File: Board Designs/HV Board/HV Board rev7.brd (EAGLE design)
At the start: 118.6 x 71.4 mm, 58 parts, among them IC1 OKI-78SR, IC2 NE5532SOIC

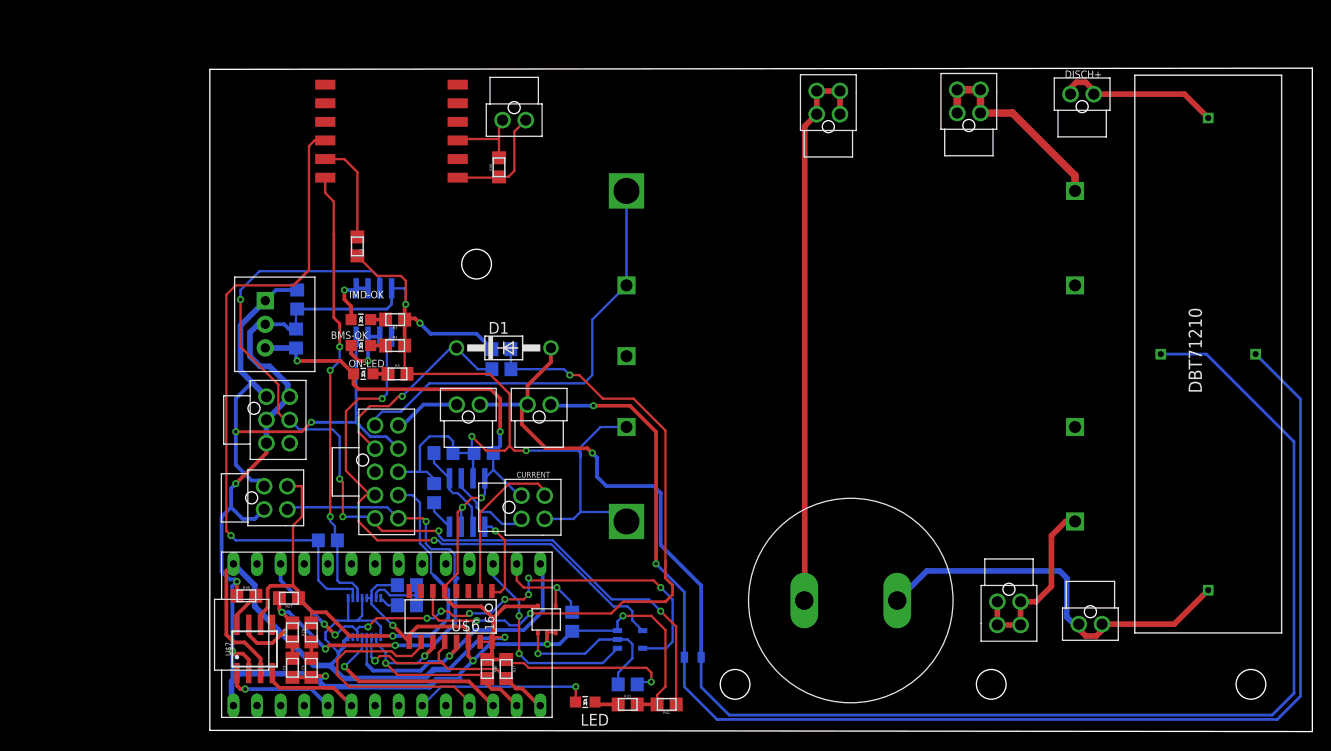
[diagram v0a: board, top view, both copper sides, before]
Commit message: Updated cynergy relay in lib, fixed DRC issues
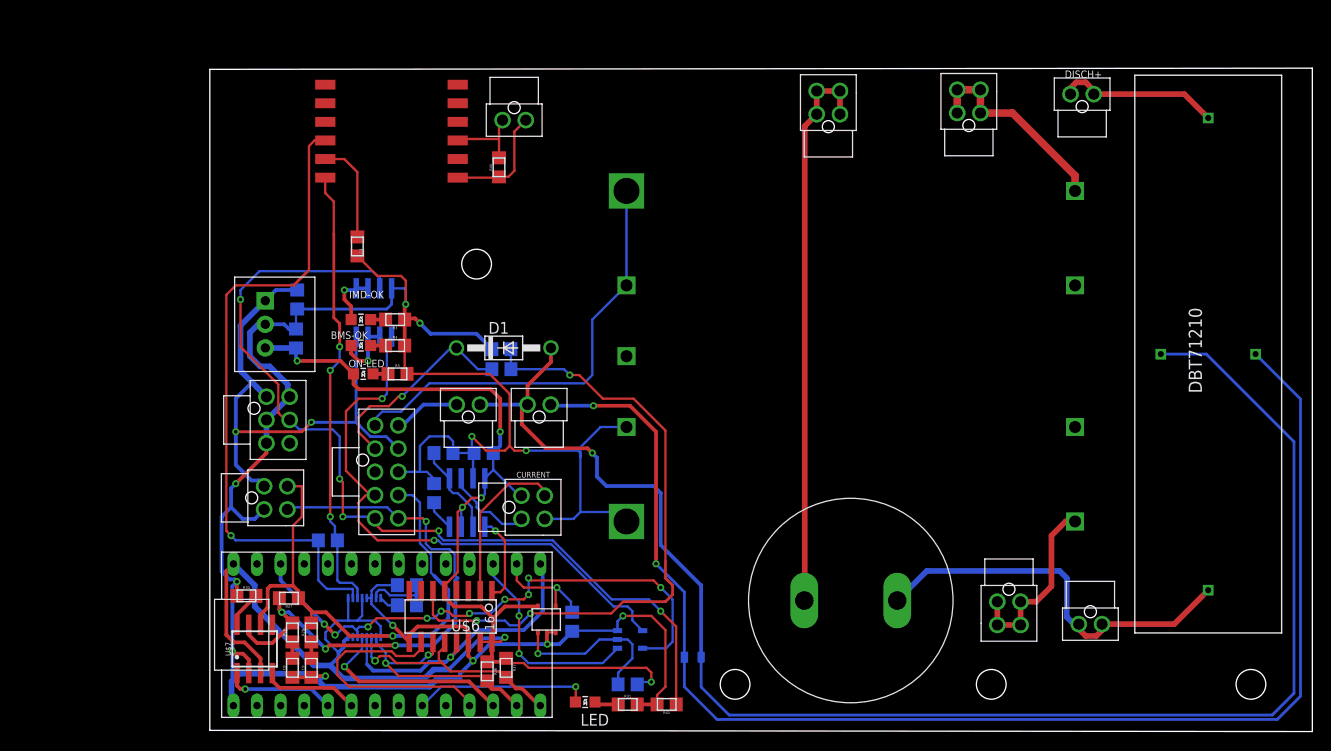
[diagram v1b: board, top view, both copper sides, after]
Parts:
- moved R36 0.25 mm to (50.4, 1.14)
- moved R37 0.13 mm to (52.5, 1.52)
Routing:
- net N$24: track 70.7 -> 69.7 mm
- net MOSI: track 26.0 -> 26.8 mm
- net N$34: track 48.8 -> 48.3 mm

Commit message: Moved 6820 next to transformer
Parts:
- IMD: value IMD -> CONNECTOR-6NANO-FIT_VERTICAL-6
- moved HV-FUSED_1A-IMD- 53.9 mm to (94.9, 61.2), turned to 0 degrees
- moved R33 38.5 mm to (31.4, 45.3), turned to 0 degrees
- moved R34 34.4 mm to (31.4, 43.2), turned to 180 degrees
- moved U$8 32.7 mm to (30.4, 37.0)
- moved R35 28.5 mm to (27.4, 43.2)
- moved C2 8.13 mm to (38.1, 41.4)
- moved C3 8.13 mm to (38.0, 37.2)
- moved IC1 8.13 mm to (34.7, 38.7)
- moved C1 6.54 mm to (96.0, 9.76)
- moved BMS-OK 5.35 mm to (42.2, 36.6)
- moved IC2 5.35 mm to (43.6, 40.1)
- moved IMD-OK 5.35 mm to (42.2, 39.4)
- moved R3 5.35 mm to (45.8, 39.4)
- moved R4 5.35 mm to (45.8, 36.6)
- moved ON-LED 5.35 mm to (42.4, 33.5)
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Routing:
- net N$33: track 70.4 -> 21.1 mm
- net CS_LTC6820: track 21.7 -> 64.0 mm
- net HV-FUSED_1A: track 20.6 -> 61.9 mm
- net SCK: track 31.9 -> 69.1 mm
- net MISO: track 25.7 -> 61.2 mm
- net MOSI: track 26.8 -> 61.5 mm
- net N$34: track 48.3 -> 15.8 mm, vias 3 -> 1
- net +3V3: track 60.5 -> 87.7 mm, vias 10 -> 8
- net GND: track 271.2 -> 249.5 mm
- net HV+UNFUSED: track 42.9 -> 29.4 mm
- net +5V: track 171.9 -> 159.3 mm
- net OKHS: track 98.3 -> 86.2 mm, vias 5 -> 4
- net +12V: track 59.0 -> 54.7 mm, vias 2 -> 1
- net N$31: track 2.12 -> 5.79 mm
- net BMS_OK: track 62.3 -> 59.1 mm
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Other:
- outline, holes or cut-outs redrawn
- board text added: "IMD"

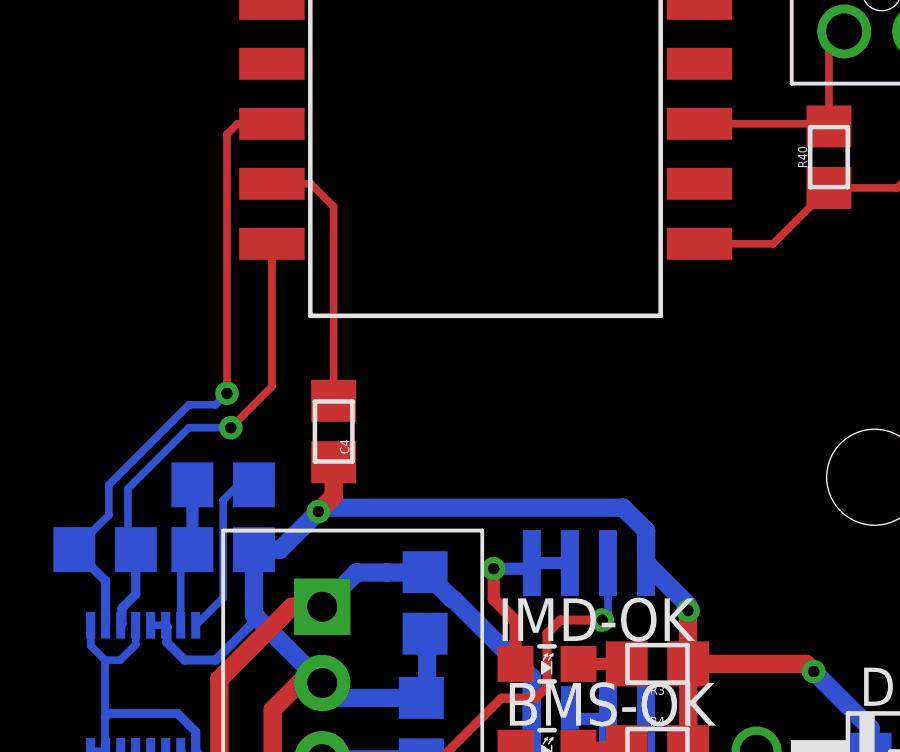
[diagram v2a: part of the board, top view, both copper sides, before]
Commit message: Moved resistor to clear space for the box
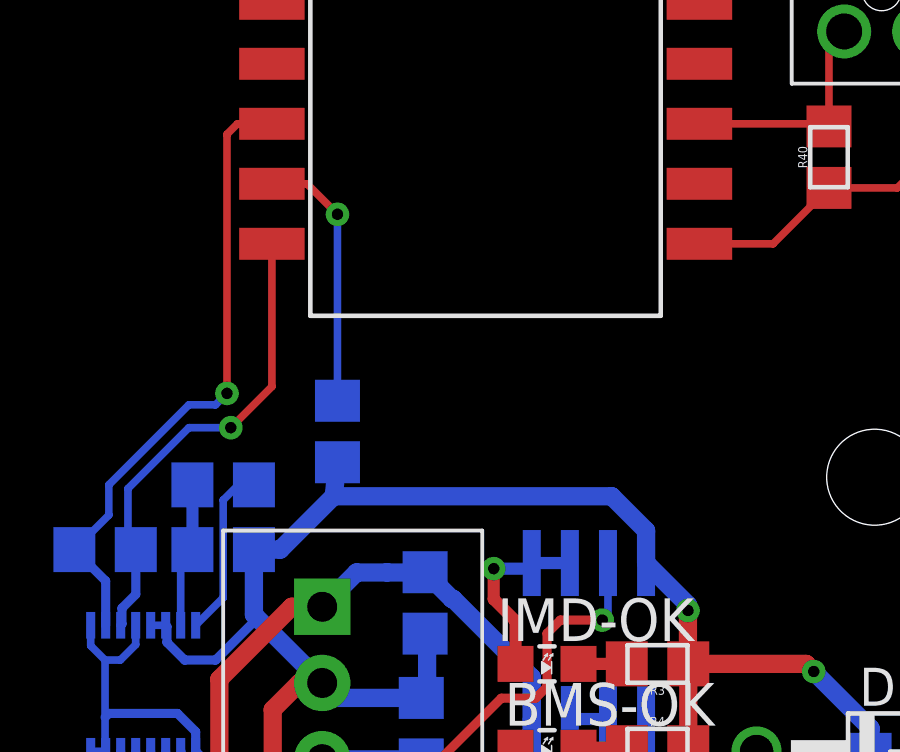
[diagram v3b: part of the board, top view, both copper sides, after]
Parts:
- moved C4 0.13 mm to (35.2, 47.1), flipped to the bottom
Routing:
- net GND: track 249.5 -> 249.1 mm, vias 12 -> 11
- net N$35: track 8.84 -> 8.82 mm, vias 0 -> 1
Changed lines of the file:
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@@
 <attribute name="VALUE" x="27.432" y="43.8912" size="0.3048" layer="28" rot="MR180" align="top-center"/>
 </element>
-<element name="C4" library="HyTechDevices" package="0805" value="27pF" x="35.052" y="47.117" smashed="yes" rot="R270">
-<attribute name="NAME" x="35.2679" y="46.609" size="0.3048" layer="25" rot="R270" align="bottom-center"/>
-<attribute name="VALUE" x="34.3408" y="47.117" size="0.3048" layer="27" rot="R270" align="top-center"/>
+<element name="C4" library="HyTechDevices" package="0805" value="27pF" x="35.179" y="47.117" smashed="yes" rot="MR270">
+<attribute name="NAME" x="34.9631" y="46.609" size="0.3048" layer="26" rot="MR270" align="bottom-center"/>
+<attribute name="VALUE" x="35.8902" y="47.117" size="0.3048" layer="28" rot="MR270" align="top-center"/>
 </element>
 <element name="R36" library="HyTechDevices" package="0805" value="2k" x="50.419" y="1.143" smashed="yes" rot="R270">
@@
 <wire x1="31.115" y1="39.497" x2="32.394" y2="40.776" width="0.3048" layer="16"/>
 <wire x1="32.394" y1="40.776" x2="32.394" y2="41.012" width="0.3048" layer="16"/>
-<wire x1="32.394" y1="43.18" x2="33.274" y2="43.18" width="0.6096" layer="16"/>
-<wire x1="33.274" y1="43.18" x2="34.544" y2="44.45" width="0.6096" layer="16"/>
-<via x="34.544" y="44.45" extent="1-16" drill="0.381"/>
-<wire x1="34.544" y1="44.45" x2="35.052" y2="44.958" width="0.6096" layer="1"/>
-<wire x1="35.052" y1="44.958" x2="35.052" y2="46.092" width="0.6096" layer="1"/>
-<wire x1="45.466" y1="42.732" x2="45.466" y2="43.815" width="0.6096" layer="16"/>
-<wire x1="45.466" y1="43.815" x2="44.704" y2="44.577" width="0.6096" layer="16"/>
-<wire x1="44.704" y1="44.577" x2="34.671" y2="44.577" width="0.6096" layer="16"/>
-<wire x1="34.671" y1="44.577" x2="34.544" y2="44.45" width="0.6096" layer="16"/>
+<wire x1="33.274" y1="43.18" x2="32.394" y2="43.18" width="0.6096" layer="16"/>
+<wire x1="35.179" y1="46.092" x2="35.052" y2="44.958" width="0.6096" layer="16"/>
+<wire x1="45.466" y1="43.815" x2="45.466" y2="42.732" width="0.6096" layer="16"/>
 <wire x1="45.466" y1="42.732" x2="46.863" y2="41.335" width="0.6096" layer="16"/>
 <wire x1="46.863" y1="41.335" x2="46.863" y2="41.148" width="0.6096" layer="16"/>
@@
 <wire x1="50.41" y1="24.511" x2="50.292" y2="24.393" width="0.6096" layer="16"/>
 <wire x1="50.292" y1="24.393" x2="50.292" y2="21.777" width="0.6096" layer="16"/>
+<wire x1="35.052" y1="44.958" x2="33.274" y2="43.18" width="0.6096" layer="16"/>
+<wire x1="35.052" y1="44.958" x2="44.323" y2="44.958" width="0.6096" layer="16"/>
+<wire x1="44.323" y1="44.958" x2="45.466" y2="43.815" width="0.6096" layer="16"/>
 </signal>
 <signal name="+12V">
@@
 <contactref element="C4" pad="1"/>
 <contactref element="U$2" pad="P$11"/>
-<wire x1="34.29" y1="55.372" x2="35.052" y2="54.61" width="0.254" layer="1"/>
-<wire x1="35.052" y1="48.142" x2="35.052" y2="54.61" width="0.254" layer="1"/>
-<wire x1="32.994" y1="55.373" x2="34.289" y2="55.373" width="0.254" layer="1"/>
-<wire x1="34.289" y1="55.373" x2="34.29" y2="55.372" width="0.254" layer="1"/>
+<wire x1="32.994" y1="55.373" x2="34.162" y2="55.373" width="0.254" layer="1"/>
+<wire x1="34.162" y1="55.373" x2="35.179" y2="54.356" width="0.254" layer="1"/>
+<via x="35.179" y="54.356" extent="1-16" drill="0.381"/>
+<wire x1="35.179" y1="54.356" x2="35.179" y2="48.142" width="0.254" layer="16"/>
 </signal>
 <signal name="N$36">

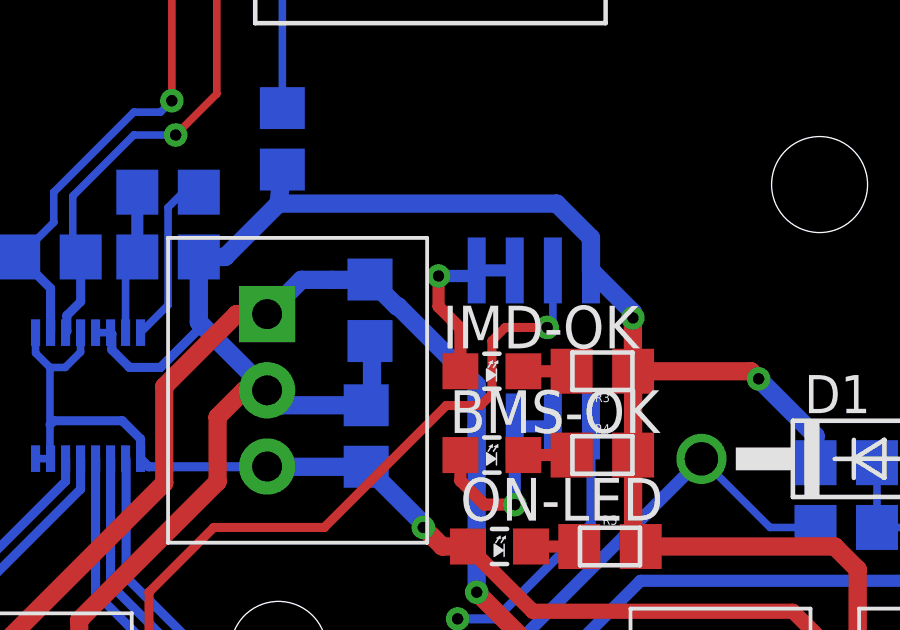
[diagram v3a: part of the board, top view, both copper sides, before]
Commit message: Fixed ISOSPI spacing issues, moved silkscreen
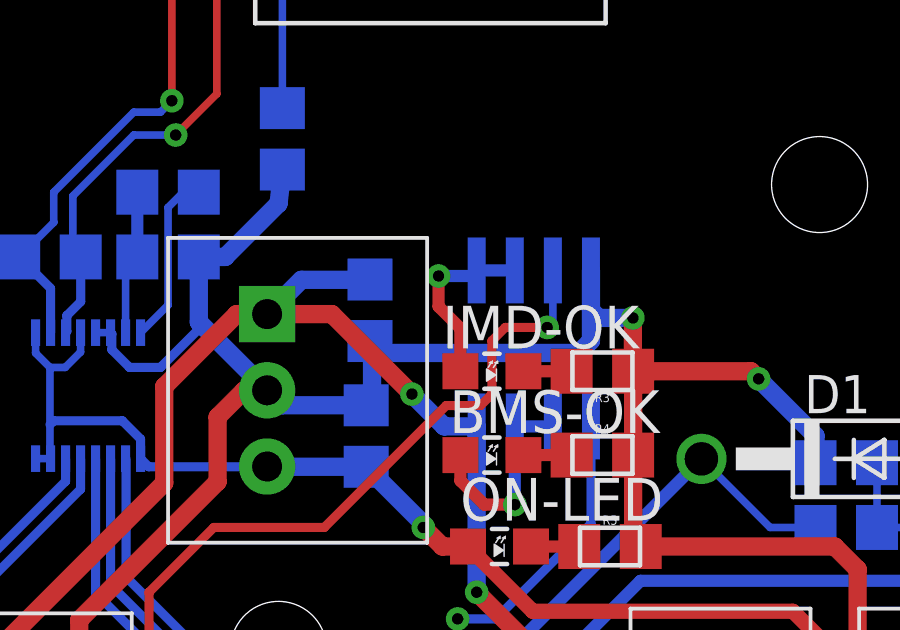
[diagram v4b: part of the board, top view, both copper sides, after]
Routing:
- net GND: track 249.1 -> 246.4 mm
- net +12V: track 54.7 -> 56.8 mm, vias 1 -> 2

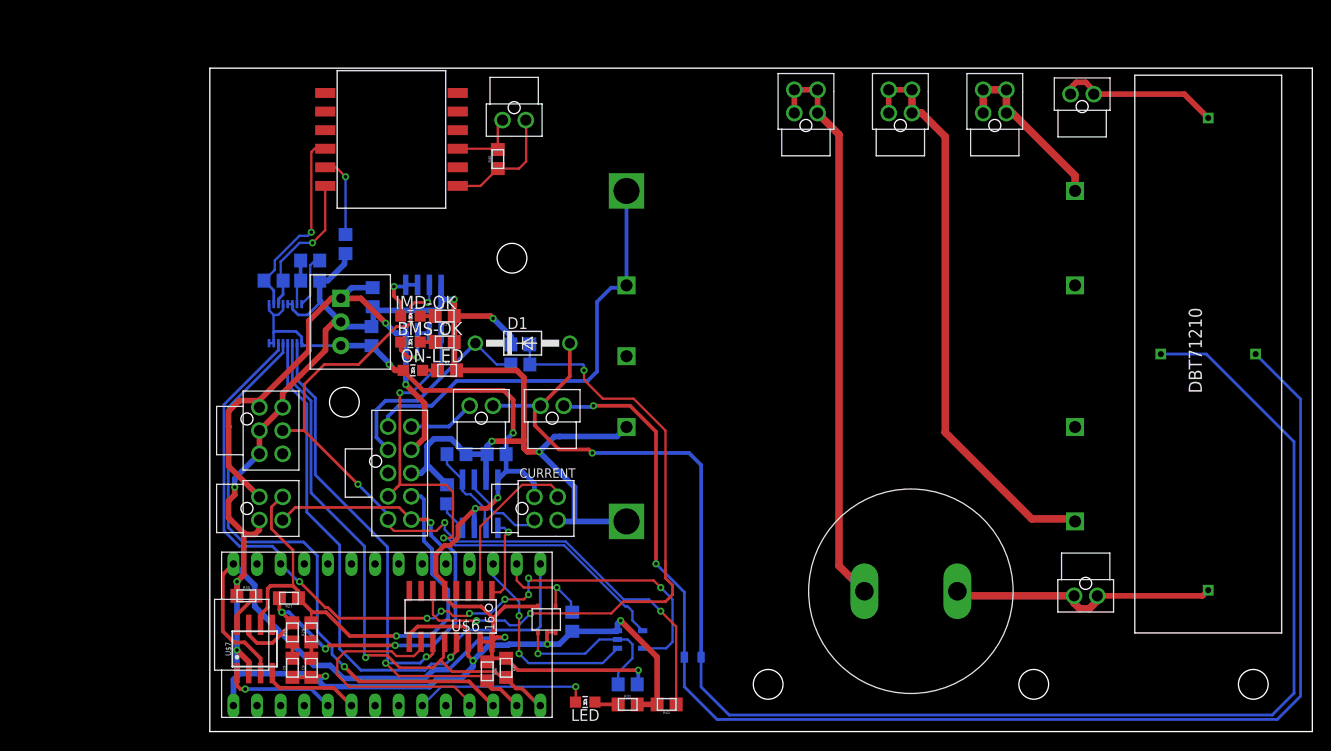
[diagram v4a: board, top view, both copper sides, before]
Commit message: Tweak HV board rev{6,7} for manufacturing
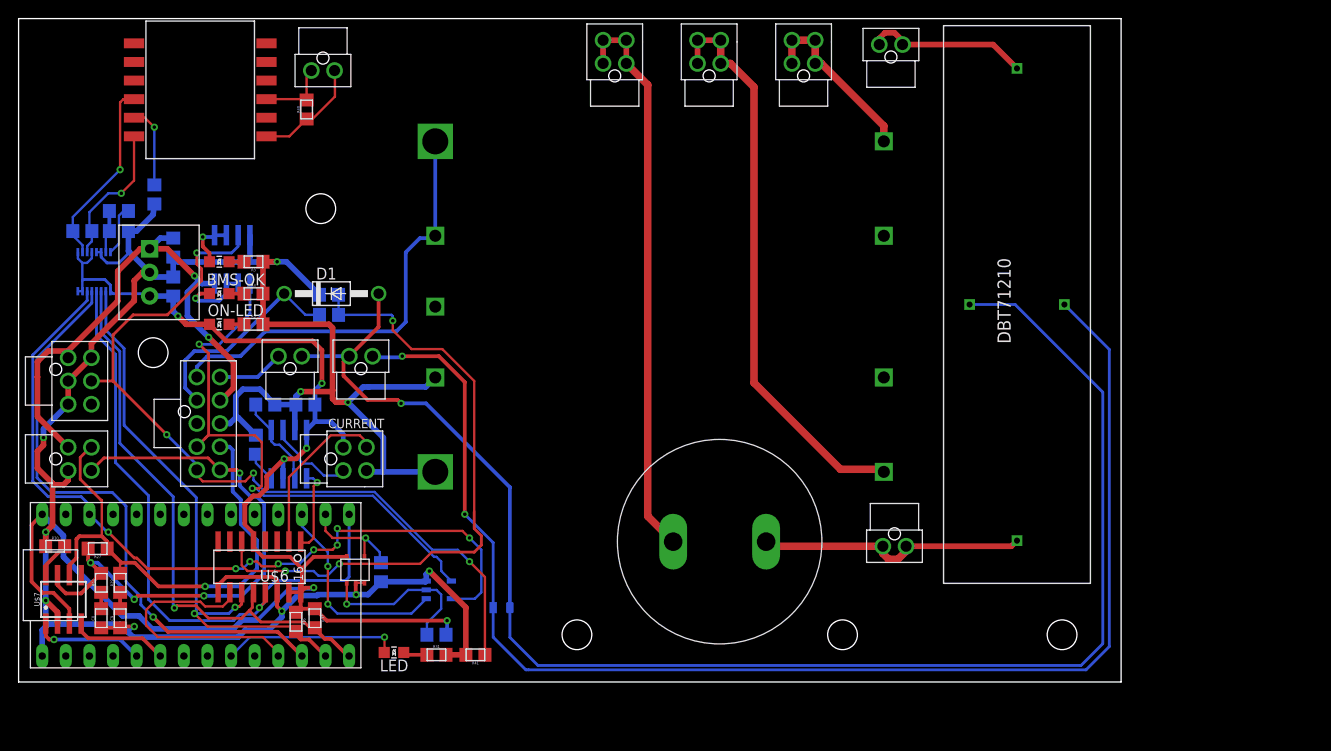
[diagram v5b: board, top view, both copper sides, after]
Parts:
- moved C2 22.1 mm to (16.6, 46.7)
- moved C3 22.0 mm to (16.6, 42.5)
- moved ON-LED 21.4 mm to (21.6, 38.5)
- moved R5 21.4 mm to (25.3, 38.5)
- moved IMD-OK 21.4 mm to (21.6, 45.2)
- moved R3 21.4 mm to (25.3, 45.2)
- moved U$8 21.3 mm to (9.78, 42.5)
- moved DISCH+ 21.3 mm to (93.9, 68.6)
- moved HV+UNFUSED 21.3 mm to (94.2, 14.6)
- moved CURRENT 21.3 mm to (34.9, 24.0)
- moved R42 21.3 mm to (39.0, 11.8)
- moved RELAYS 21.3 mm to (36.8, 35.1)
- moved U$9 21.3 mm to (36.8, 1.52)
- moved C4 21.3 mm to (14.6, 52.5)
- moved C5 21.3 mm to (30.9, 29.8)
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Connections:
- net N$33 renamed IM
- net N$34 renamed IP
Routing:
- net SHUTDOWN7: track 170.4 -> 165.9 mm
- net BMS_OK: track 59.1 -> 60.5 mm
- net +12V: track 56.8 -> 58.0 mm
- net OKHS: track 86.2 -> 87.3 mm
- net +5V: track 159.3 -> 160.3 mm
- net ISOSPI-P: track 12.9 -> 12.0 mm
- net N$43: track 6.87 -> 7.80 mm
- net GND: track 246.4 -> 247.2 mm, vias 11 -> 10
- net IM: track 21.1 -> 20.3 mm
- net N$42: track 6.09 -> 5.59 mm
